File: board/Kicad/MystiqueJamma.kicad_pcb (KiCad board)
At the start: 2 copper layers, 140.4 x 114.8 mm, 165 parts, among them IC1 7805, IC10 TDA2030V, IC11 LA4425V, IC12 CY7C1049CV33, IC2 74HC4021D, IC3 74LS245DW, IC4 74HC4021D, IC5 CY7C1049CV33, IC6 TDA1543T, IC7 74LS245DW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

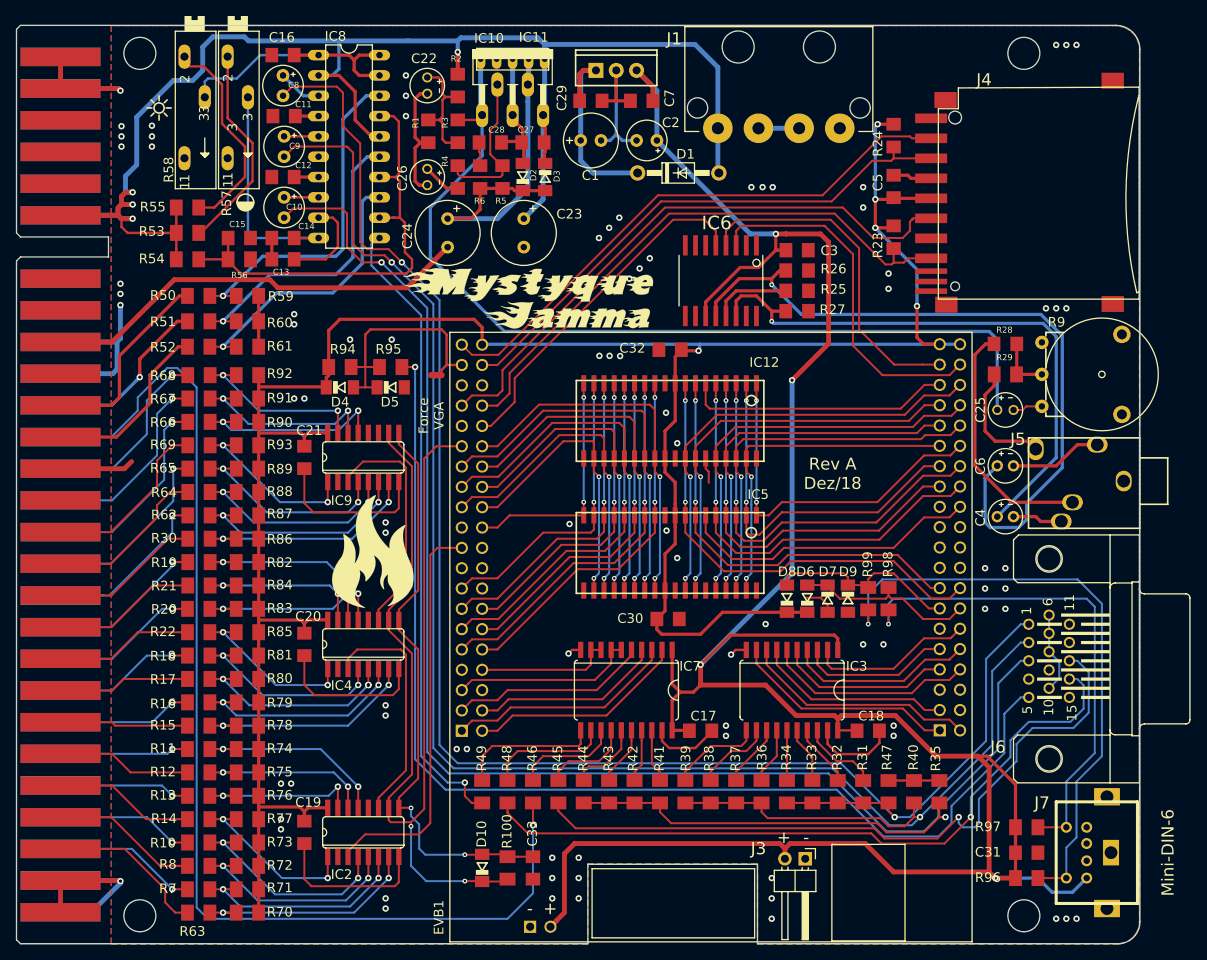
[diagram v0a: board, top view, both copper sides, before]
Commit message: Added Micro SD card connector
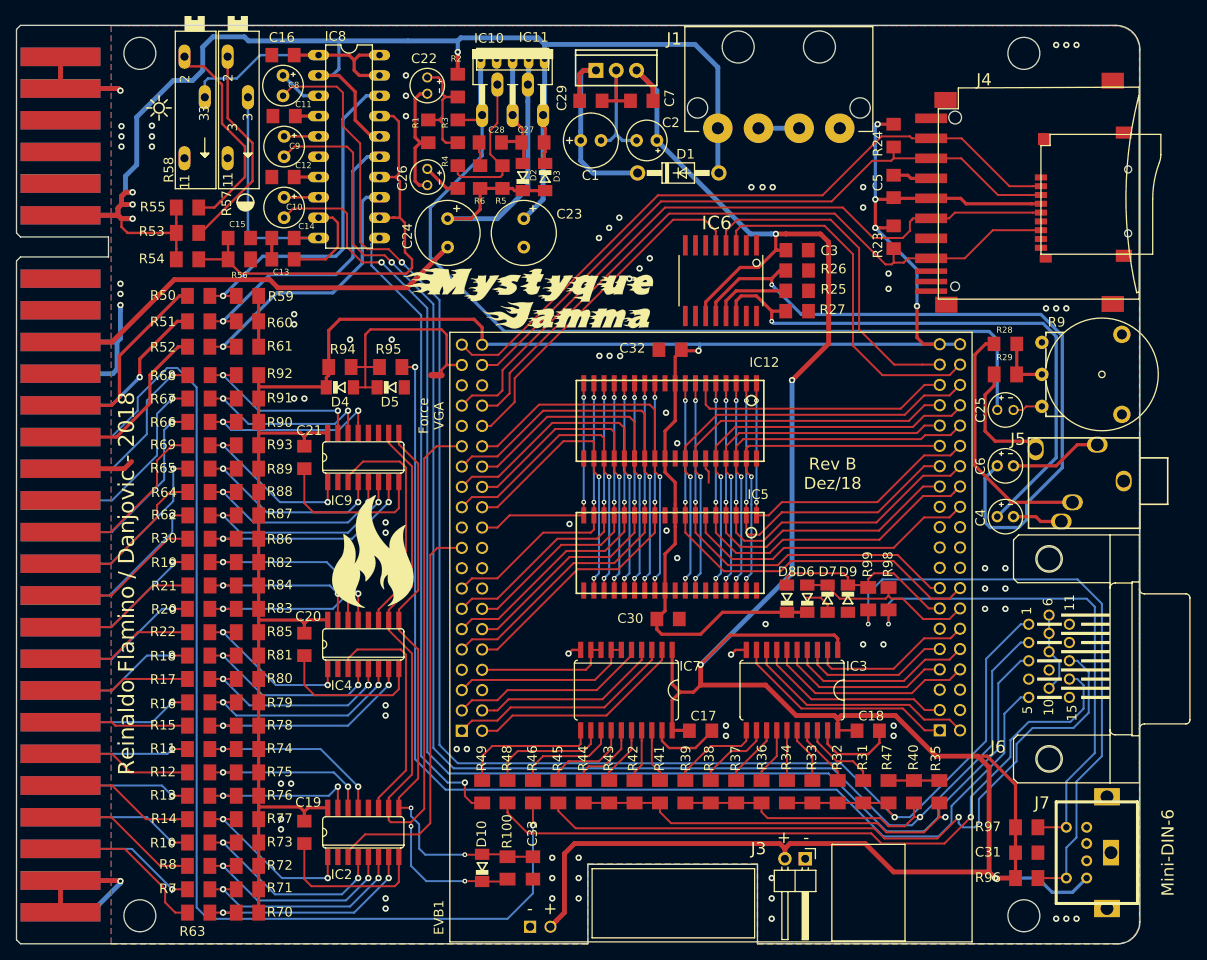
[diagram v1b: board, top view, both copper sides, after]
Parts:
- added J2: Micro_SD_Card, MystiqueJamma:9P-SMD-W_-RING, F.Cu at (194.9, 55.2)
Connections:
- J4 pad GP2: (no net) -> GND
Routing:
- net /SD_CS: track 70.6 -> 86.8 mm
- net /SD_DATAIN: track 68.2 -> 83.9 mm
- net /SD_DATAOUT: track 72.3 -> 87.4 mm
- net /SD_CNT_SCLK: track 73.7 -> 87.7 mm
- net +3V3: track 300.4 -> 314.4 mm
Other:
- board text added: "Reinaldo Flamino / Danjovic - 2018"
- board text added: "Rev B Dez/18"
- board text removed: "Rev A Dez/18"
